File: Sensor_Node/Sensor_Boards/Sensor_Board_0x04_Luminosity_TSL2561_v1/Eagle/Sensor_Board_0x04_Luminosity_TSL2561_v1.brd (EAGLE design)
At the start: 55 x 35 mm, 16 parts, among them J1 M04_SMD_90, J4 ARDUINO_ISP, U2 ATMEGA328P_TQFP, Y1 8MHZ

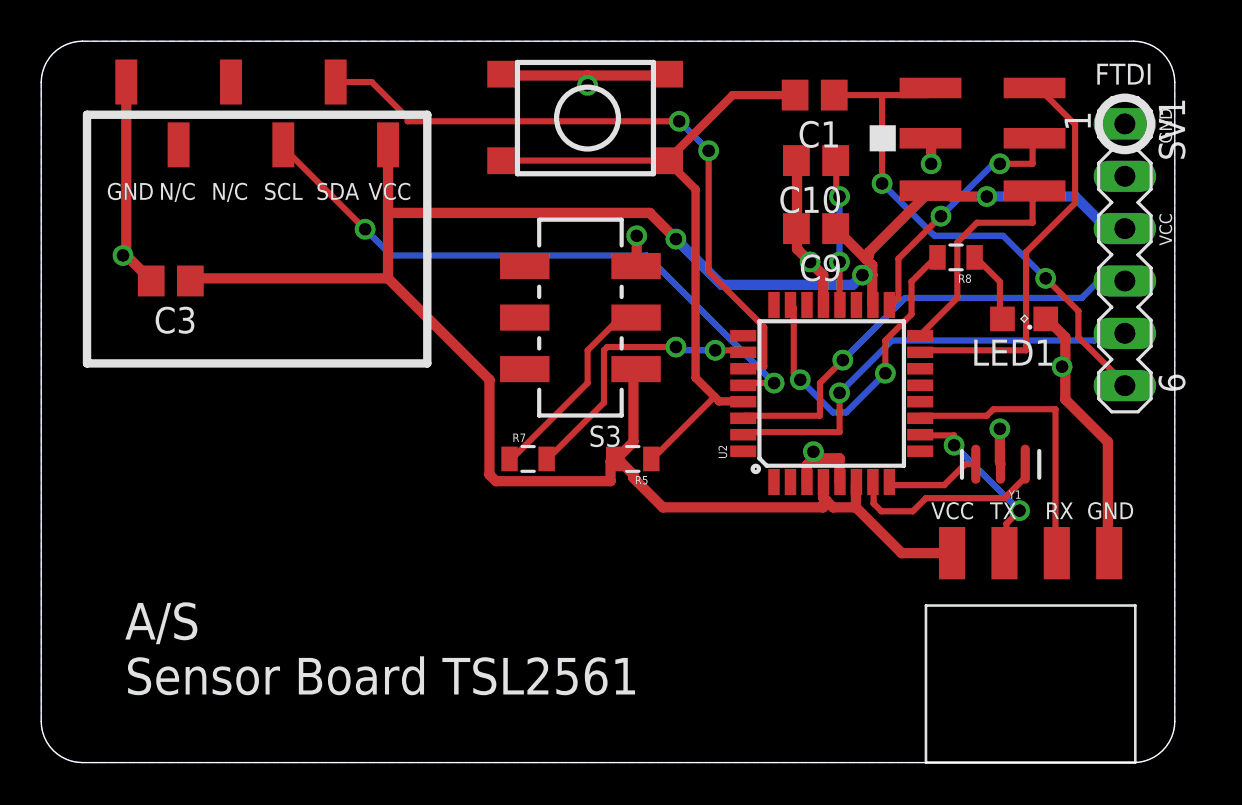
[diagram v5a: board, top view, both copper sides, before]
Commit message: TSL2561
- reset path
- sensor connector footer
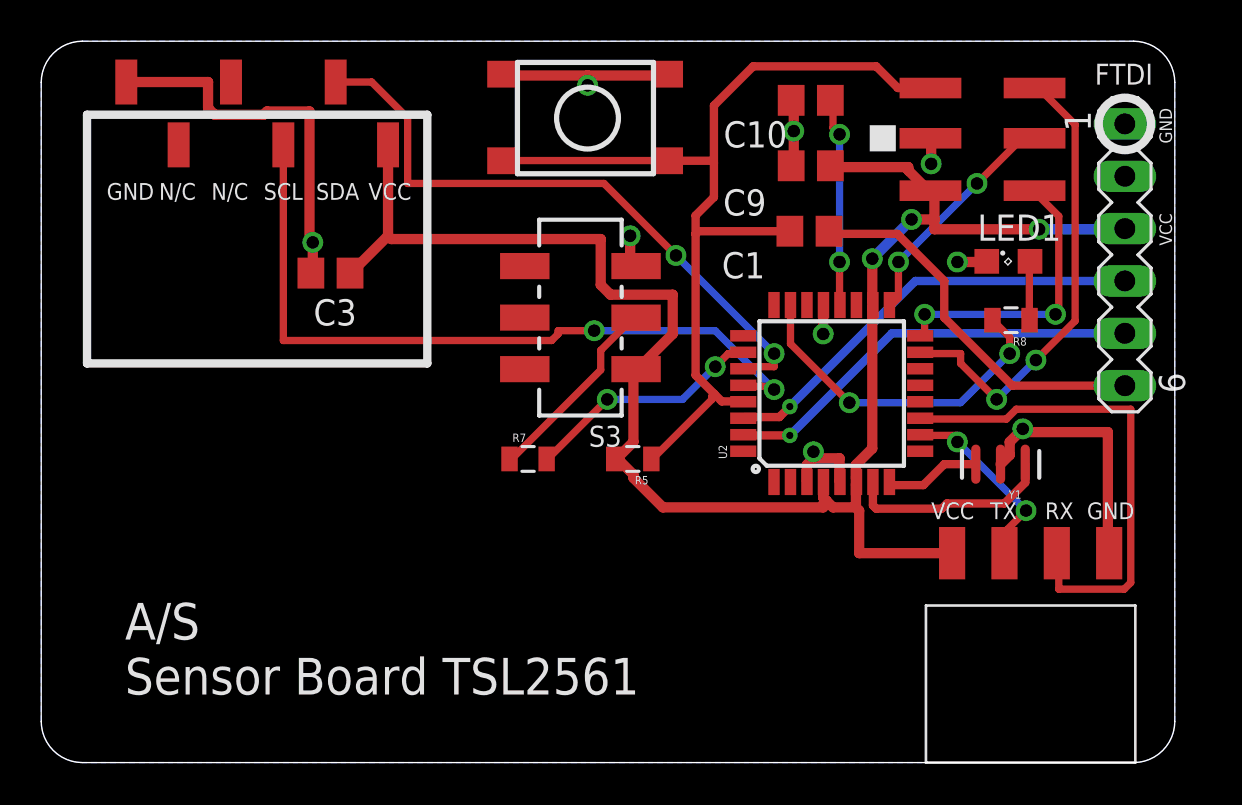
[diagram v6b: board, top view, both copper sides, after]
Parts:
- moved C3 7.76 mm to (14.0, 23.7)
- moved C1 6.61 mm to (37.3, 25.8)
- moved R8 4.05 mm to (47.1, 21.5)
- moved C9 3.06 mm to (37.3, 29.0)
- moved C10 2.93 mm to (37.3, 32.1)
- moved LED1 2.90 mm to (46.9, 24.3), turned to 0 degrees
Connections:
- removed net N$4: C1.2, R5.1, S1.3, S1.4, U2.29
- new net FTDI_RESET: C1.1, SV1.6
- net RESET: now also C1.2, R5.1, S1.3, S1.4, U2.29; no longer C1.1, SV1.6
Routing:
- net N$4: track 33.7 -> 0.00 mm
- net RESET: track 25.9 -> 47.4 mm, vias 2 -> 0
- net VCC: track 105.1 -> 86.3 mm
- net FTDI_RESET: track 0.00 -> 18.5 mm
- net MCU_RXI: track 13.8 -> 24.3 mm
- net SCL: track 30.2 -> 36.5 mm
- net GND: track 47.7 -> 52.2 mm, vias 8 -> 9
- net MISO: track 10.9 -> 14.0 mm, vias 0 -> 2
- net N$15: track 7.12 -> 10.1 mm
- net MOSI: track 20.0 -> 22.7 mm, vias 0 -> 2
- net DBG_ENABLE: track 13.4 -> 11.7 mm
- net SDA: track 32.2 -> 30.8 mm
- net FTDI_TXO: track 21.7 -> 20.6 mm
- net FTDI_RXI: track 22.2 -> 21.3 mm
- net SCK: track 12.2 -> 11.4 mm
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
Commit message: Error TSL2561
Rotated the sensor connector by 180 deg.
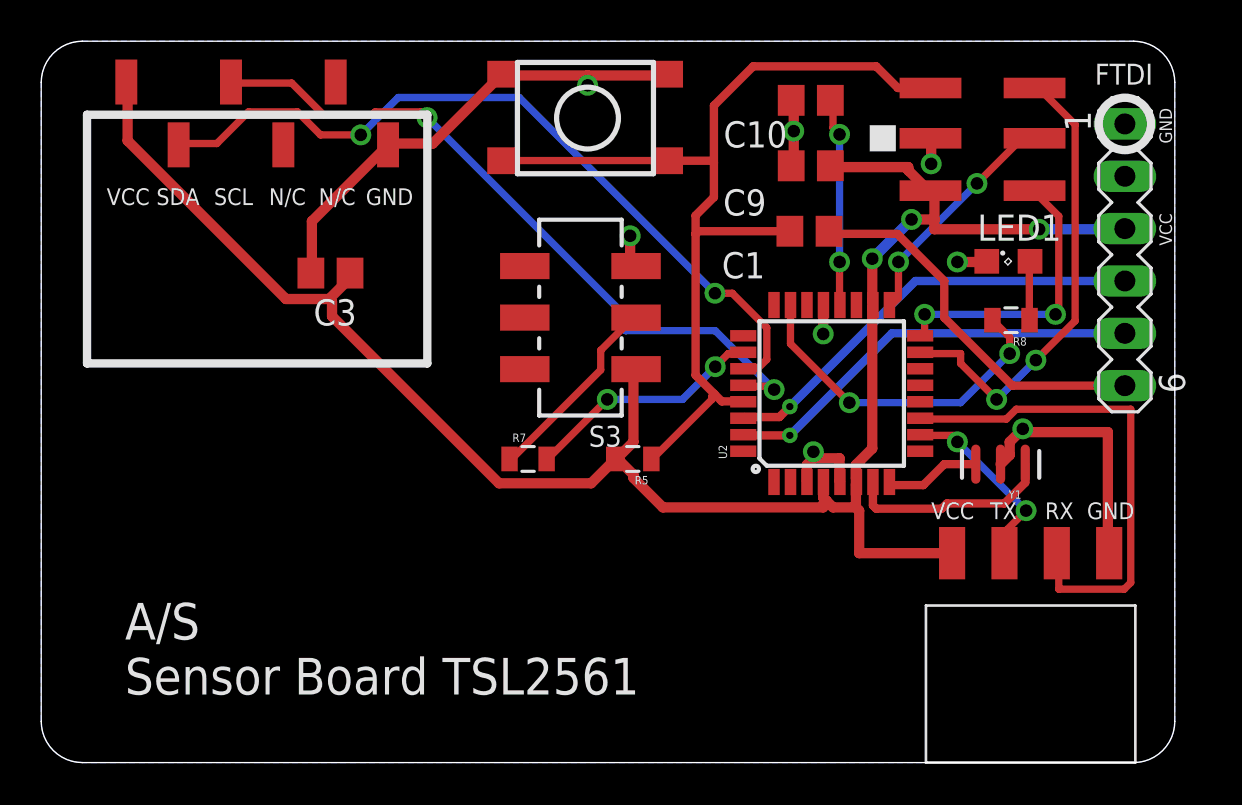
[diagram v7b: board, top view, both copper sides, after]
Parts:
- moved U$9 13.1 mm to (16.8, 30.0), turned to 180 degrees
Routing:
- net VCC: track 86.3 -> 94.7 mm
- net SDA: track 30.8 -> 37.9 mm
- net GND: track 52.2 -> 48.7 mm, vias 9 -> 8
- net SCL: track 36.5 -> 34.8 mm

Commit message: Changed Sensorboard TSL2561
- adjusted connector of comboard to a consistent distance
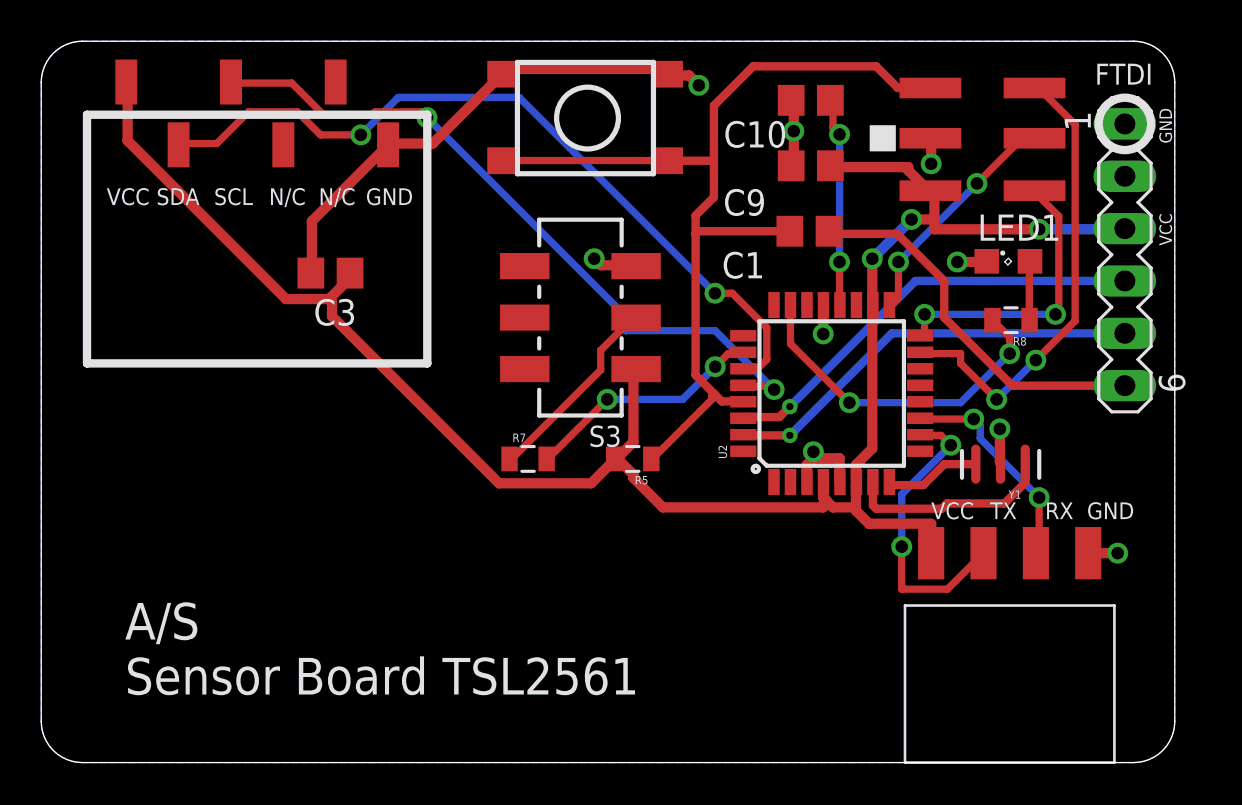
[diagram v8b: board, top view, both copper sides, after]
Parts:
- moved J1 1.02 mm to (43.2, 10.2)
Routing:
- net MCU_RXI: track 24.3 -> 10.7 mm, vias 0 -> 2
- net GND: track 48.7 -> 41.6 mm, vias 8 -> 9
- net MCU_TXO: track 9.40 -> 14.4 mm
- net VCC: track 94.7 -> 93.4 mm
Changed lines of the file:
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@@
 <text x="54.864" y="25.0825" size="0.6096" layer="21" rot="R90">VCC</text>
 <rectangle x1="40.1955" y1="29.6545" x2="41.4655" y2="30.9245" layer="21"/>
+<dimension x1="50.8" y1="10.16" x2="54.991" y2="10.16" x3="52.8955" y3="-5.588" textsize="1.778" layer="47"/>
 </plain>
 <attributes>
@@
 </element>
 <element name="S3" library="myownthings" package="JS202011SCQN" value="JS202011SCQN" x="26.162" y="21.59" rot="R90"/>
-<element name="J1" library="myownthings" package="M04_SMD_90" value="M04_SMD_90" x="44.196" y="10.16"/>
+<element name="J1" library="myownthings" package="M04_SMD_90" value="M04_SMD_90" x="43.18" y="10.16"/>
 <element name="SV1" library="con-lstb" package="MA06-1" value="" x="52.578" y="24.638" smashed="yes" rot="R270">
 <attribute name="MF" value="" x="52.578" y="24.638" size="1.778" layer="27" rot="R270" display="off"/>
@@
 <contactref element="SV1" pad="2"/>
 <contactref element="U$9" pad="P1"/>
-<wire x1="46.99" y1="14.9225" x2="46.5455" y2="14.478" width="0.5" layer="1"/>
-<wire x1="46.99" y1="15.5575" x2="46.99" y2="14.9225" width="0.5" layer="1"/>
-<wire x1="47.46625" y1="16.03375" x2="46.99" y2="15.5575" width="0.5" layer="1"/>
-<wire x1="51.7525" y1="16.03375" x2="47.46625" y2="16.03375" width="0.5" layer="1"/>
-<wire x1="51.7525" y1="10.16" x2="51.7525" y2="16.03375" width="0.5" layer="1"/>
-<wire x1="51.7525" y1="10.16" x2="51.816" y2="10.16" width="0.5" layer="1"/>
-<wire x1="30.32125" y1="33.3375" x2="26.51125" y2="33.3375" width="0.5" layer="1"/>
-<wire x1="26.51125" y1="33.3375" x2="22.5425" y2="33.3375" width="0.5" layer="1"/>
-<wire x1="22.5425" y1="33.3375" x2="22.4155" y2="33.401" width="0.5" layer="1"/>
-<wire x1="30.32125" y1="33.3375" x2="30.3655" y2="33.401" width="0.5" layer="1"/>
 <wire x1="36.5125" y1="32.0675" x2="36.5125" y2="30.63875" width="0.5" layer="1"/>
 <wire x1="36.5125" y1="30.63875" x2="36.5125" y2="29.05125" width="0.5" layer="1"/>
@@
 <wire x1="37.94125" y1="22.06625" x2="37.954" y2="22.1996" width="0.5" layer="1"/>
 <wire x1="37.465" y1="15.08125" x2="37.465" y2="14.76375" width="0.5" layer="1"/>
-<wire x1="28.575" y1="24.28875" x2="28.73375" y2="24.13" width="0.5" layer="1"/>
-<wire x1="28.575" y1="25.55875" x2="28.575" y2="24.28875" width="0.5" layer="1"/>
-<wire x1="28.73375" y1="24.13" x2="28.862" y2="24.09" width="0.5" layer="1"/>
 <wire x1="43.18" y1="29.05125" x2="43.18" y2="30.1625" width="0.5" layer="1"/>
 <wire x1="43.18" y1="30.1625" x2="43.1465" y2="30.2895" width="0.5" layer="1"/>
-<wire x1="26.51125" y1="32.86125" x2="26.51125" y2="33.3375" width="0.5" layer="1"/>
-<wire x1="47.625" y1="16.1925" x2="47.46625" y2="16.03375" width="0.5" layer="1"/>
 <via x="44.45" y="24.28875" extent="1-16" drill="0.6096"/>
 <via x="37.94125" y="20.79625" extent="1-16" drill="0.6096"/>
 <via x="37.465" y="15.08125" extent="1-16" drill="0.6096"/>
-<via x="28.575" y="25.55875" extent="1-16" drill="0.6096"/>
 <via x="36.5125" y="30.63875" extent="1-16" drill="0.6096"/>
 <via x="43.18" y="29.05125" extent="1-16" drill="0.6096"/>
-<via x="26.51125" y="32.86125" extent="1-16" drill="0.6096"/>
-<via x="47.625" y="16.1925" extent="1-16" drill="0.6096"/>
 <wire x1="13.1318" y1="26.2636" x2="13.1318" y2="23.749" width="0.5" layer="1"/>
 <wire x1="16.764" y1="29.8958" x2="13.1318" y2="26.2636" width="0.5" layer="1"/>
@@
 <wire x1="17.0434" y1="30.0355" x2="16.8275" y2="29.972" width="0.5" layer="1"/>
 <wire x1="22.2123" y1="33.2486" x2="22.4155" y2="33.401" width="0.5" layer="1"/>
+<wire x1="31.4325" y1="33.3375" x2="30.48" y2="33.3375" width="0.5" layer="1"/>
+<wire x1="31.90875" y1="32.86125" x2="31.4325" y2="33.3375" width="0.5" layer="1"/>
+<wire x1="30.48" y1="33.3375" x2="30.3655" y2="33.401" width="0.5" layer="1"/>
+<wire x1="30.00375" y1="33.655" x2="30.1625" y2="33.49625" width="0.5" layer="1"/>
+<wire x1="22.38375" y1="33.655" x2="30.00375" y2="33.655" width="0.5" layer="1"/>
+<wire x1="30.1625" y1="33.49625" x2="30.3655" y2="33.401" width="0.5" layer="1"/>
+<wire x1="22.38375" y1="33.655" x2="22.4155" y2="33.401" width="0.5" layer="1"/>
+<wire x1="46.51375" y1="16.1925" x2="46.51375" y2="14.605" width="0.5" layer="1"/>
+<wire x1="46.51375" y1="14.605" x2="46.5455" y2="14.478" width="0.5" layer="1"/>
+<wire x1="27.14625" y1="24.13" x2="28.73375" y2="24.13" width="0.5" layer="1"/>
+<wire x1="26.82875" y1="24.4475" x2="27.14625" y2="24.13" width="0.5" layer="1"/>
+<wire x1="28.73375" y1="24.13" x2="28.862" y2="24.09" width="0.5" layer="1"/>
+<wire x1="52.22875" y1="10.16" x2="50.8" y2="10.16" width="0.5" layer="1"/>
+<via x="31.90875" y="32.86125" extent="1-16" drill="0.6096"/>
+<via x="46.51375" y="16.1925" extent="1-16" drill="0.6096"/>
+<via x="26.82875" y="24.4475" extent="1-16" drill="0.6096"/>
+<via x="52.22875" y="10.16" extent="1-16" drill="0.6096"/>
 </signal>
 <signal name="VCC" class="1">
@@
 <wire x1="40.3225" y1="22.06625" x2="40.354" y2="22.1996" width="0.5" layer="1"/>
 <wire x1="39.52875" y1="13.81125" x2="39.554" y2="13.6144" width="0.5" layer="1"/>
-<wire x1="39.6875" y1="10.16" x2="44.196" y2="10.16" width="0.5" layer="1"/>
-<wire x1="39.6875" y1="12.22375" x2="39.6875" y2="10.16" width="0.5" layer="1"/>
-<wire x1="39.6875" y1="12.22375" x2="39.52875" y2="12.3825" width="0.5" layer="1"/>
 <wire x1="28.73375" y1="13.97" x2="28.09875" y2="14.605" width="0.5" layer="1"/>
 <wire x1="28.73375" y1="13.81125" x2="28.73375" y2="13.97" width="0.5" layer="1"/>
@@
 <wire x1="14.1097" y1="22.352" x2="13.97" y2="22.4917" width="0.5" layer="1"/>
 <wire x1="27.6606" y1="14.5288" x2="27.802" y2="14.732" width="0.5" layer="1"/>
+<wire x1="43.18" y1="11.58875" x2="43.18" y2="10.16" width="0.5" layer="1"/>
+<wire x1="40.16375" y1="11.58875" x2="43.18" y2="11.58875" width="0.5" layer="1"/>
+<wire x1="39.52875" y1="12.22375" x2="40.16375" y2="11.58875" width="0.5" layer="1"/>
+<wire x1="39.52875" y1="12.22375" x2="39.52875" y2="12.3825" width="0.5" layer="1"/>
 </signal>
 <signal name="RESET">
@@
 <contactref element="J1" pad="2"/>
 <contactref element="U2" pad="10"/>
-<wire x1="44.45" y1="15.875" x2="42.70375" y2="15.875" width="0.3556" layer="1"/>
-<wire x1="44.45" y1="15.5575" x2="44.45" y2="15.875" width="0.3556" layer="1"/>
-<wire x1="47.78375" y1="12.22375" x2="44.45" y2="15.5575" width="0.3556" layer="16"/>
-<wire x1="46.83125" y1="11.27125" x2="47.78375" y2="12.22375" width="0.3556" layer="1"/>
-<wire x1="46.83125" y1="10.16" x2="46.83125" y2="11.27125" width="0.3556" layer="1"/>
+<wire x1="43.65625" y1="15.875" x2="42.70375" y2="15.875" width="0.3556" layer="1"/>
+<wire x1="44.1325" y1="15.39875" x2="43.65625" y2="15.875" width="0.3556" layer="1"/>
+<wire x1="41.75125" y1="13.0175" x2="44.1325" y2="15.39875" width="0.3556" layer="16"/>
+<wire x1="41.75125" y1="10.4775" x2="41.75125" y2="13.0175" width="0.3556" layer="16"/>
+<wire x1="41.75125" y1="8.41375" x2="41.75125" y2="10.4775" width="0.3556" layer="1"/>
+<wire x1="43.97375" y1="8.41375" x2="41.75125" y2="8.41375" width="0.3556" layer="1"/>
+<wire x1="45.72" y1="10.16" x2="43.97375" y2="8.41375" width="0.3556" layer="1"/>
 <wire x1="42.70375" y1="15.875" x2="42.6466" y2="15.907" width="0.3556" layer="1"/>
-<wire x1="46.83125" y1="10.16" x2="46.736" y2="10.16" width="0.3556" layer="1"/>
-<via x="44.45" y="15.5575" extent="1-16" drill="0.6096"/>
-<via x="47.78375" y="12.22375" extent="1-16" drill="0.6096"/>
+<via x="44.1325" y="15.39875" extent="1-16" drill="0.6096"/>
+<via x="41.75125" y="10.4775" extent="1-16" drill="0.6096"/>
 </signal>
 <signal name="SCL">
@@
 <contactref element="J1" pad="3"/>
 <contactref element="U2" pad="11"/>
-<wire x1="46.83125" y1="16.66875" x2="42.70375" y2="16.66875" width="0.3556" layer="1"/>
-<wire x1="47.3075" y1="17.145" x2="46.83125" y2="16.66875" width="0.3556" layer="1"/>
-<wire x1="52.86375" y1="17.145" x2="47.3075" y2="17.145" width="0.3556" layer="1"/>
-<wire x1="52.86375" y1="8.73125" x2="52.86375" y2="17.145" width="0.3556" layer="1"/>
-<wire x1="52.54625" y1="8.41375" x2="52.86375" y2="8.73125" width="0.3556" layer="1"/>
-<wire x1="49.37125" y1="8.41375" x2="52.54625" y2="8.41375" width="0.3556" layer="1"/>
-<wire x1="49.37125" y1="10.16" x2="49.37125" y2="8.41375" width="0.3556" layer="1"/>
 <wire x1="42.70375" y1="16.66875" x2="42.6466" y2="16.707" width="0.3556" layer="1"/>
-<wire x1="49.37125" y1="10.16" x2="49.276" y2="10.16" width="0.3556" layer="1"/>
+<wire x1="45.24375" y1="16.66875" x2="42.8625" y2="16.66875" width="0.3556" layer="1"/>
+<wire x1="45.56125" y1="16.35125" x2="45.24375" y2="16.66875" width="0.3556" layer="16"/>
+<wire x1="45.56125" y1="15.71625" x2="45.56125" y2="16.35125" width="0.3556" layer="16"/>
+<wire x1="48.41875" y1="12.85875" x2="45.56125" y2="15.71625" width="0.3556" layer="16"/>
+<wire x1="48.41875" y1="10.16" x2="48.41875" y2="12.85875" width="0.3556" layer="1"/>
+<wire x1="48.26" y1="10.16" x2="48.41875" y2="10.16" width="0.3556" layer="1"/>
+<wire x1="42.8625" y1="16.66875" x2="42.6466" y2="16.707" width="0.3556" layer="1"/>
+<via x="45.24375" y="16.66875" extent="1-16" drill="0.6096"/>
+<via x="48.41875" y="12.85875" extent="1-16" drill="0.6096"/>
 </signal>
 <signal name="DBG_ENABLE">
